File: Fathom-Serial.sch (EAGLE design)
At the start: 113 parts, among them IC1 LMH6643, IC2 LMH6643, IC3 ST490AB, IC4 ST490AB, IC5 FT230XS, Q1 BC817-40W, U1 MC7812, U2 MC7805, U4 INA139, U5 MC7805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

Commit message: Increased termination resistor size appropriately for RS485. Hopefully we can get by without using these eventually.
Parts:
- removed R27, R30: 86.6, SparkFun:RESISTOR0603-RES
- added R15, R16: NP, resistor:R-US_R1210
- R26, R28, R29, R31: value 43 -> 0; device SparkFun:RESISTOR0603-RES -> SparkFun:RESISTOR1206
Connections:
- net ROV-TP3+: now also R16.2; no longer R30.1
- net ROV-TP3-: now also R16.1; no longer R30.2
- net TOP-TP2+: now also R15.2; no longer R27.1
- net TOP-TP2-: now also R15.1; no longer R27.2
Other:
- note added: "Termination resistors removed to minimize power losses. If required, use: Series resistors: 43 ohm 1/4 W Parallel resistor: 86.6 ohm, 1/2 W"
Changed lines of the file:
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@@
 <part name="IC3" library="maxim" deviceset="MAX488" device="CSA" value="ST490AB"/>
 <part name="GND7" library="SparkFun" deviceset="GND" device=""/>
-<part name="R26" library="SparkFun" deviceset="RESISTOR" device="0603-RES" value="43"/>
-<part name="R27" library="SparkFun" deviceset="RESISTOR" device="0603-RES" value="86.6"/>
-<part name="R28" library="SparkFun" deviceset="RESISTOR" device="0603-RES" value="43"/>
+<part name="R26" library="SparkFun" deviceset="RESISTOR" device="1206" value="0"/>
+<part name="R28" library="SparkFun" deviceset="RESISTOR" device="1206" value="0"/>
 <part name="GND-ISO4" library="SparkFun-Aesthetics" deviceset="GND-ISO" device=""/>
 <part name="GND-ISO5" library="SparkFun-Aesthetics" deviceset="GND-ISO" device=""/>
@@
 <part name="C22" library="SparkFun" deviceset="CAP" device="0603-CAP" value="0.1uF"/>
 <part name="IC4" library="maxim" deviceset="MAX488" device="CSA" value="ST490AB"/>
-<part name="R29" library="SparkFun" deviceset="RESISTOR" device="0603-RES" value="43"/>
-<part name="R30" library="SparkFun" deviceset="RESISTOR" device="0603-RES" value="86.6"/>
-<part name="R31" library="SparkFun" deviceset="RESISTOR" device="0603-RES" value="43"/>
+<part name="R29" library="SparkFun" deviceset="RESISTOR" device="1206" value="0"/>
+<part name="R31" library="SparkFun" deviceset="RESISTOR" device="1206" value="0"/>
 <part name="GND-ISO16" library="SparkFun-Aesthetics" deviceset="GND-ISO" device=""/>
 <part name="GND-ISO17" library="SparkFun-Aesthetics" deviceset="GND-ISO" device=""/>
@@
 <part name="U2" library="SparkFun-PowerIC" deviceset="V_REG_MC33269" device="DT" value="MC7805"/>
 <part name="JP4" library="SparkFun-Connectors" deviceset="M02" device="PTH" value="0.1&quot; HEADER"/>
+<part name="R15" library="resistor" deviceset="R-US_" device="R1210" value="NP"/>
+<part name="R16" library="resistor" deviceset="R-US_" device="R1210" value="NP"/>
 </parts>
 <sheets>
@@
 <wire x1="147.32" y1="35.56" x2="147.32" y2="55.88" width="0.1524" layer="94"/>
 <wire x1="147.32" y1="55.88" x2="0" y2="55.88" width="0.1524" layer="94"/>
+<text x="182.88" y="63.5" size="1.778" layer="97">Termination resistors removed to
+minimize power losses. If required, use:
+Series resistors: 43 ohm 1/4 W
+Parallel resistor: 86.6 ohm, 1/2 W</text>
 </plain>
 <instances>
@@
 <instance part="GND7" gate="1" x="91.44" y="68.58"/>
 <instance part="R26" gate="G$1" x="170.18" y="86.36"/>
-<instance part="R27" gate="G$1" x="172.72" y="68.58" rot="R270"/>
 <instance part="R28" gate="G$1" x="170.18" y="93.98"/>
 <instance part="C22" gate="G$1" x="20.32" y="30.48"/>
@@
 <instance part="IC4" gate="P" x="35.56" y="30.48"/>
 <instance part="R29" gate="G$1" x="114.3" y="33.02"/>
-<instance part="R30" gate="G$1" x="116.84" y="15.24" rot="R270"/>
 <instance part="R31" gate="G$1" x="114.3" y="40.64"/>
 <instance part="GND-ISO16" gate="G$1" x="20.32" y="22.86"/>
 <instance part="GND-ISO17" gate="G$1" x="35.56" y="15.24"/>
+<instance part="R15" gate="G$1" x="172.72" y="68.58" rot="R90"/>
+<instance part="R16" gate="G$1" x="116.84" y="15.24" rot="R90"/>
 </instances>
 <busses>
@@
 <segment>
 <pinref part="IC4" gate="G$1" pin="A"/>
-<pinref part="R30" gate="G$1" pin="1"/>
 <wire x1="83.82" y1="22.86" x2="116.84" y2="22.86" width="0.1524" layer="91"/>
 <wire x1="116.84" y1="22.86" x2="116.84" y2="20.32" width="0.1524" layer="91"/>
 <label x="93.98" y="22.86" size="1.778" layer="95"/>
+<pinref part="R16" gate="G$1" pin="2"/>
 </segment>
 </net>
@@
 <segment>
 <pinref part="IC3" gate="G$1" pin="A"/>
-<pinref part="R27" gate="G$1" pin="1"/>
 <wire x1="139.7" y1="76.2" x2="172.72" y2="76.2" width="0.1524" layer="91"/>
 <wire x1="172.72" y1="76.2" x2="172.72" y2="73.66" width="0.1524" layer="91"/>
 <label x="149.86" y="76.2" size="1.778" layer="95"/>
+<pinref part="R15" gate="G$1" pin="2"/>
 </segment>
 </net>
@@
 <wire x1="139.7" y1="71.12" x2="165.1" y2="71.12" width="0.1524" layer="91"/>
 <label x="149.86" y="71.12" size="1.778" layer="95"/>
-<pinref part="R27" gate="G$1" pin="2"/>
 <wire x1="172.72" y1="63.5" x2="172.72" y2="60.96" width="0.1524" layer="91"/>
 <wire x1="172.72" y1="60.96" x2="165.1" y2="60.96" width="0.1524" layer="91"/>
 <wire x1="165.1" y1="60.96" x2="165.1" y2="71.12" width="0.1524" layer="91"/>
+<pinref part="R15" gate="G$1" pin="1"/>
 </segment>
 </net>
@@
 <wire x1="83.82" y1="17.78" x2="109.22" y2="17.78" width="0.1524" layer="91"/>
 <label x="93.98" y="17.78" size="1.778" layer="95"/>
-<pinref part="R30" gate="G$1" pin="2"/>
 <wire x1="116.84" y1="10.16" x2="116.84" y2="7.62" width="0.1524" layer="91"/>
 <wire x1="116.84" y1="7.62" x2="109.22" y2="7.62" width="0.1524" layer="91"/>
 <wire x1="109.22" y1="7.62" x2="109.22" y2="17.78" width="0.1524" layer="91"/>
-</segment>
-</net>
+<pinref part="R16" gate="G$1" pin="1"/>
+</segment>
+</net>

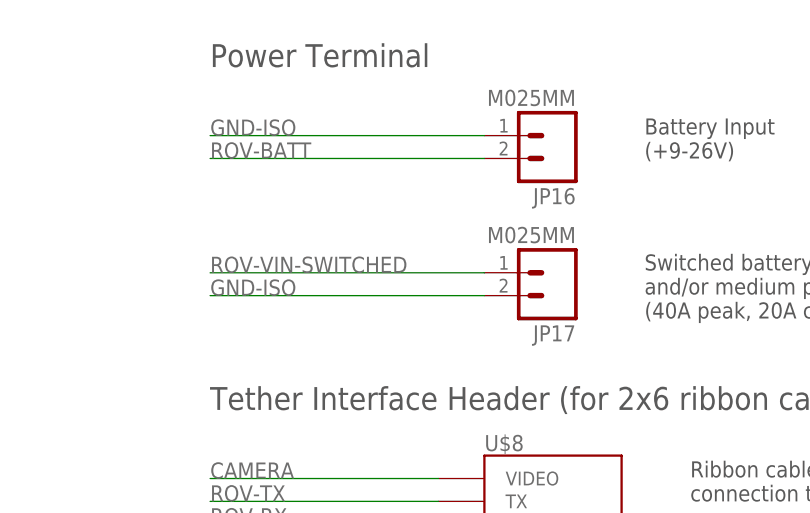
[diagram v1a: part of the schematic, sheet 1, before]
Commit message: Updated tether ribbon header size and pinout.
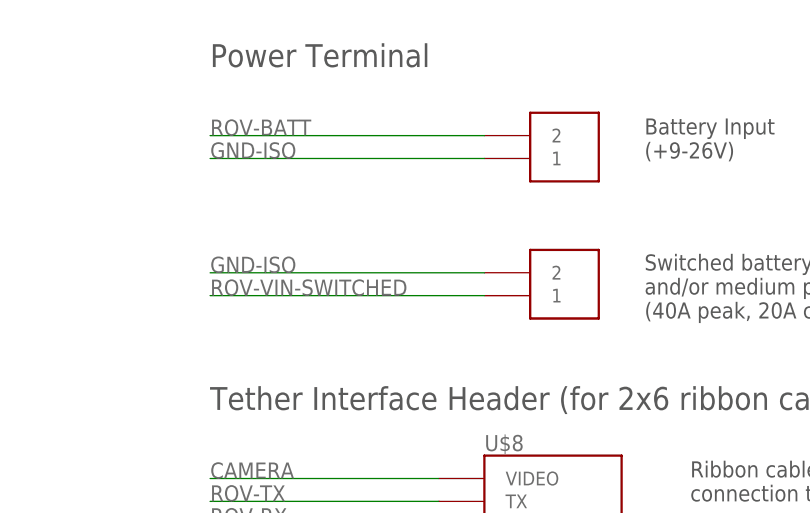
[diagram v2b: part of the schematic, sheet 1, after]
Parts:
- removed JP14: 1935161, SparkFun-Connectors:M025MM
- removed JP16, JP17: M025MM, SparkFun-Connectors:M025MM
- added U$10, U$11, U$12: HEADER-2, BR-Eagle-Library:HEADER-2
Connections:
- net GND: now also U$12.1; no longer JP14.1
- net GND-ISO: now also U$10.1, U$11.2; no longer JP16.1, JP17.2
- net ROV-BATT: now also U$10.2; no longer JP16.2
- net ROV-VIN-SWITCHED: now also U$11.1; no longer JP17.1
- net TOP-VIN: now also U$12.2; no longer JP14.2

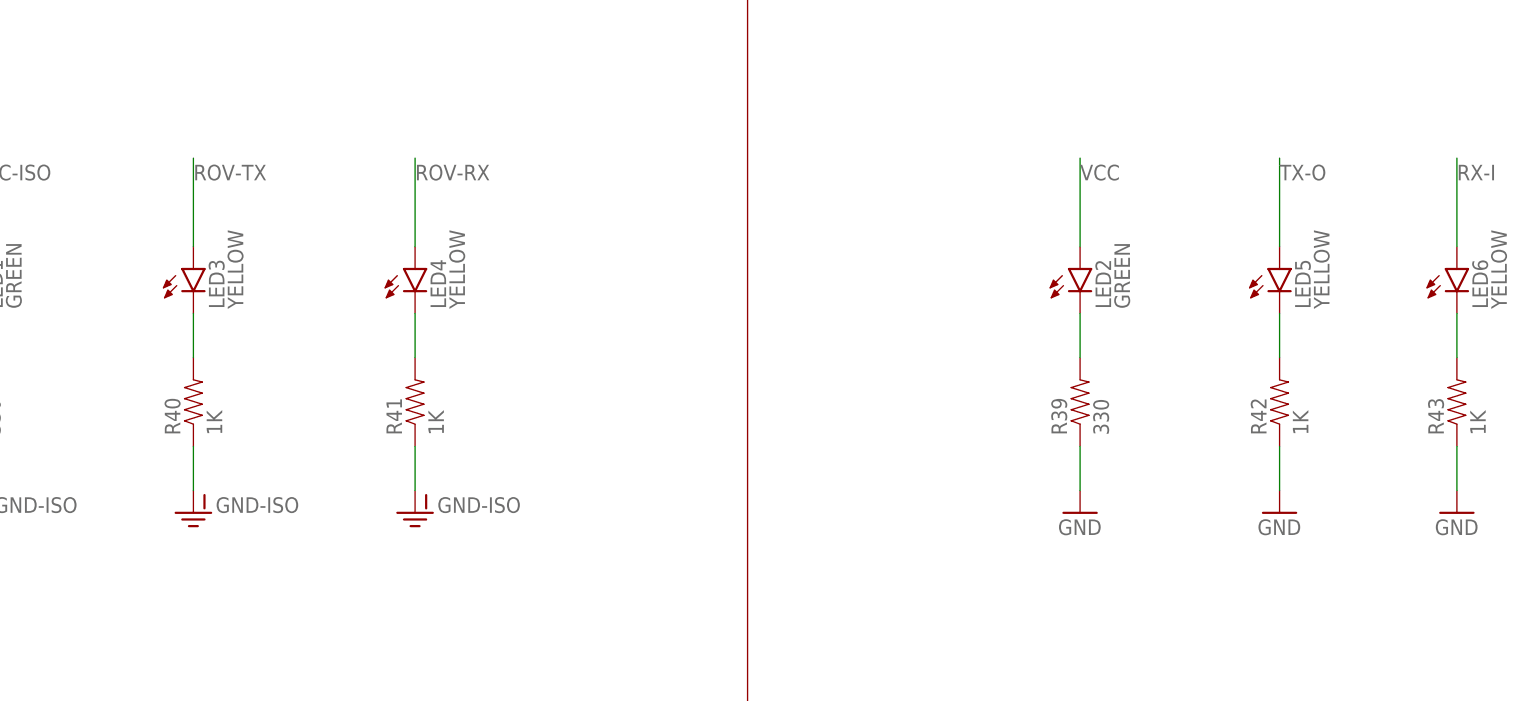
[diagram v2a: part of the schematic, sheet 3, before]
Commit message: Lots of changes based on testing of first prototype. Fixed regulators, removed RX/TX leds, added RTS reset, changed negative supply capacitors.
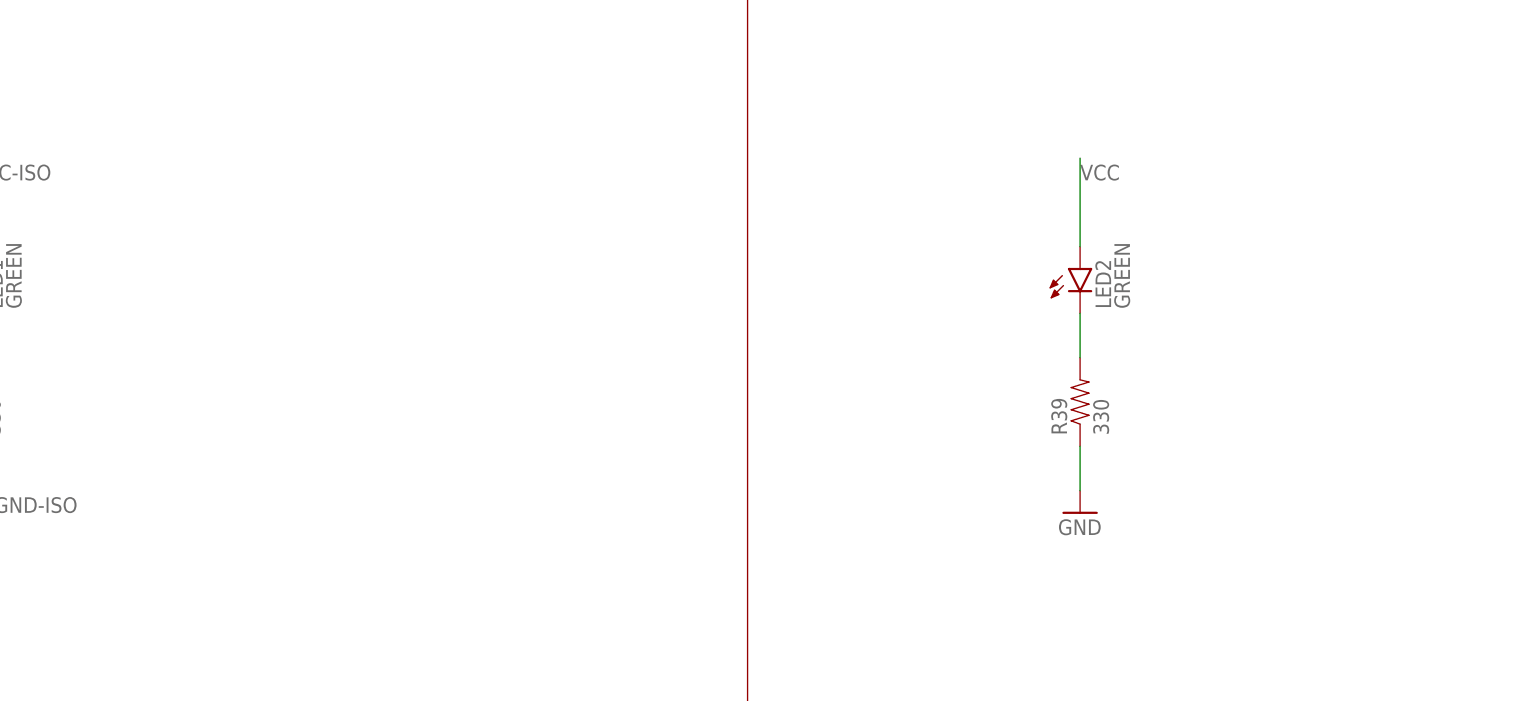
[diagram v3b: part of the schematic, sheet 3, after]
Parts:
- removed LED3, LED4, LED5, LED6: YELLOW, SparkFun-LED:LED0603
- removed R40, R41, R42, R43: 1K, SparkFun-Resistors:33KOHM1/10W1%(0603)
- added R17: 10K, SparkFun:RESISTOR0603-RES
- added SJ4: JUMPER-PAD-2-NC_BY_PASTE, SparkFun-Passives:JUMPER-PAD-2-NC_BY_PASTE
- C11: value 0.1uF -> 1uF; device SparkFun-Passives:CAP0603-CAP -> SparkFun:CAP0603-CAP
- C12, C6: value 2.2uF -> 2.2uF X5R; device SparkFun-Passives:CAP_POL1206 -> SparkFun-Passives:CAP0603-CAP
- C14, C7: value 0.1uF -> 2.2uF X5R
- C5, C9: value 1uF -> 1uF X5R
- F1: device SparkFun:PTCSMD -> SparkFun:PTC0603
- JP1, JP6: device SparkFun-Connectors:RCA -> BR-Eagle-Library:RCA
- U1, U2, U5: device SparkFun-PowerIC:V_REG_MC33269DT -> BR-Eagle-Library:78XX
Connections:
- removed net N$34: LED3.C, R40.2
- removed net N$35: LED4.C, R41.2
- removed net N$36: LED5.C, R42.2
- removed net N$37: LED6.C, R43.2
- new net N$7: C11.1, SJ4.2
- new net ROV-ON-CTRL: C11.2, JP7.7, R17.1
- new net RTS: IC5.!RTS, SJ4.1
- net -VCC: now also C6.1; no longer C12.-
- net -VCC-ISO: now also C12.1; no longer C6.-
- net GND: now also C6.2; no longer C12.+, R42.1, R43.1
- net GND-ISO: now also C12.2; no longer C11.2, C6.+, R40.1, R41.1
- net ROV-RX: no longer LED4.A
- net ROV-TX: no longer LED3.A
- net ROV-VIN: no longer C11.1
- net RX-I: no longer LED6.A
- net TX-O: no longer LED5.A
- net VCC: now also R17.2; no longer JP7.7
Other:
- note added: "Capacitively coupled reset circuitry to allow programming of Arduino boards."
